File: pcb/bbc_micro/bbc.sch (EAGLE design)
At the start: 16 parts, among them J1 ATX24RH

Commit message: added one more -5v rail
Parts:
- added U$5: BLADE28, blade:BLADE28
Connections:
- net N$2: now also U$5.P$1
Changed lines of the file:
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@@
 <part name="GND1" library="supply1" library_urn="urn:adsk.eagle:library:371" deviceset="GND" device=""/>
 <part name="P+2" library="supply1" library_urn="urn:adsk.eagle:library:371" deviceset="+5V" device=""/>
+<part name="U$5" library="blade" deviceset="BLADE28" device=""/>
 </parts>
 <sheets>
@@
 <attribute name="VALUE" x="-12.7" y="165.1" size="1.778" layer="96" rot="R90"/>
 </instance>
+<instance part="U$5" gate="G$1" x="185.42" y="101.6" smashed="yes"/>
 </instances>
 <busses>
@@
 <junction x="157.48" y="96.52"/>
 <pinref part="U$2" gate="G$1" pin="P$1"/>
-<wire x1="157.48" y1="96.52" x2="175.26" y2="96.52" width="0.1524" layer="91"/>
-</segment>
-</net>
+<wire x1="157.48" y1="96.52" x2="170.18" y2="96.52" width="0.1524" layer="91"/>
+<pinref part="U$5" gate="G$1" pin="P$1"/>
+<wire x1="170.18" y1="96.52" x2="175.26" y2="96.52" width="0.1524" layer="91"/>
+<wire x1="175.26" y1="101.6" x2="170.18" y2="101.6" width="0.1524" layer="91"/>
+<wire x1="170.18" y1="101.6" x2="170.18" y2="96.52" width="0.1524" layer="91"/>
+<junction x="170.18" y="96.52"/>
+</segment>
+</net>

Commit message: BBC micro USB adaptor
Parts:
- removed IC1: (no value), v-reg:79XXS
- removed J1: ATX24RH, macse:ATX24RH
- removed JP2: (no value), pinhead:PINHD-1X3
- removed U$1: CAR_FUSE_HOLDER3IN1, atx_power_control:CAR_FUSE_HOLDER3IN1
- removed U$2: BLADE28, blade:BLADE28
- added C1, C8: 100nF, clock:CAP0805
- added C2, C4, C6: 1uF, clock:CAP0805
- added C5: 2.2uF, clock:CAP0805
- added C7: (no value), adafruit:CPOL-USE2.5-6
- added R1, R2: 5K1, atx_power_control:RESISTOR0805-RES
- added U1, U3: TPS60400DVBR, TPS6040x:TPS60400DVBR
- added U2: USBC_16P, my_usbc_16p:USBC_16P
- C3: value (none) -> 1uF; device capacitor-wima:C5/2.5 -> clock:CAP0805
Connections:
- removed net +12V: J1.12V@0, JP2.3
- removed net -12V: IC1.IN, J1.-12V
- removed net N$6: J1.5V@1, J1.5V@2, J1.5V@3, J1.5V@4, JP2.1, U$1.B0, U$1.B1
- new net -5V: C5.1, C8.2, U$5.P$1, U1.OUT, U3.OUT
- new net N$3: C3.1, U3.C1+
- new net N$31: R1.1, U2.CC2
- new net N$33: R2.1, U2.CC1
- new net N$4: C4.2, U1.C1-
- net +5V: now also C1.2, C2.2, C6.2, C7.+, JP1.1, JP3.2_VCC, U$3.P$2, U$3.P$4, U1.IN, U3.IN; no longer U$1.A0, U$1.A1
- net GND: now also C1.1, C2.1, C5.2, C6.1, C7.-, C8.1, R1.2, R2.2, U1.GND, U2.GND, U3.GND; no longer C3.2, IC1.GND, J1.GND@0, J1.GND@1, J1.GND@2, J1.GND@3, J1.GND@4, J1.GND@5, J1.GND@6, J1.GND@7, JP1.2, U$3.P$1, U$3.P$3
- net N$1: now also JP1.2, U$3.P$1, U$3.P$3, U2.VBUS; no longer JP2.2, JP3.2_VCC
- net N$2: now also C3.2, U3.C1-; no longer C3.1, IC1.OUT, U$2.P$1, U$5.P$1
- net N$5: now also C4.1, U1.C1+; no longer J1.PS_ON, JP1.1, U$3.P$2, U$3.P$4
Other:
- moved on the sheet: C3, JP1

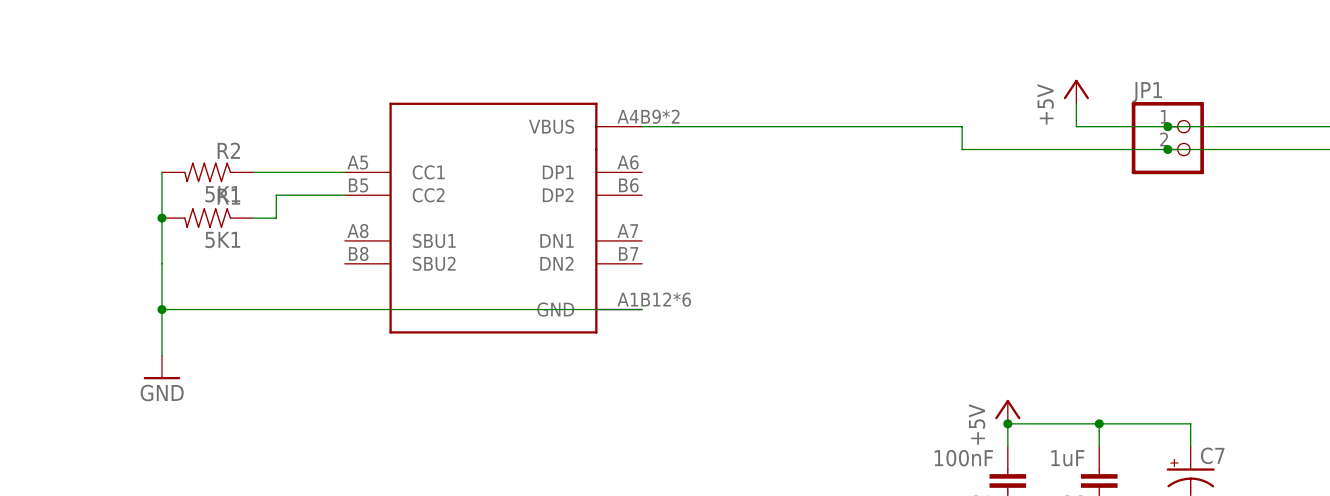
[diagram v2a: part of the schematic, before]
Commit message: BBC micro USB adaptor
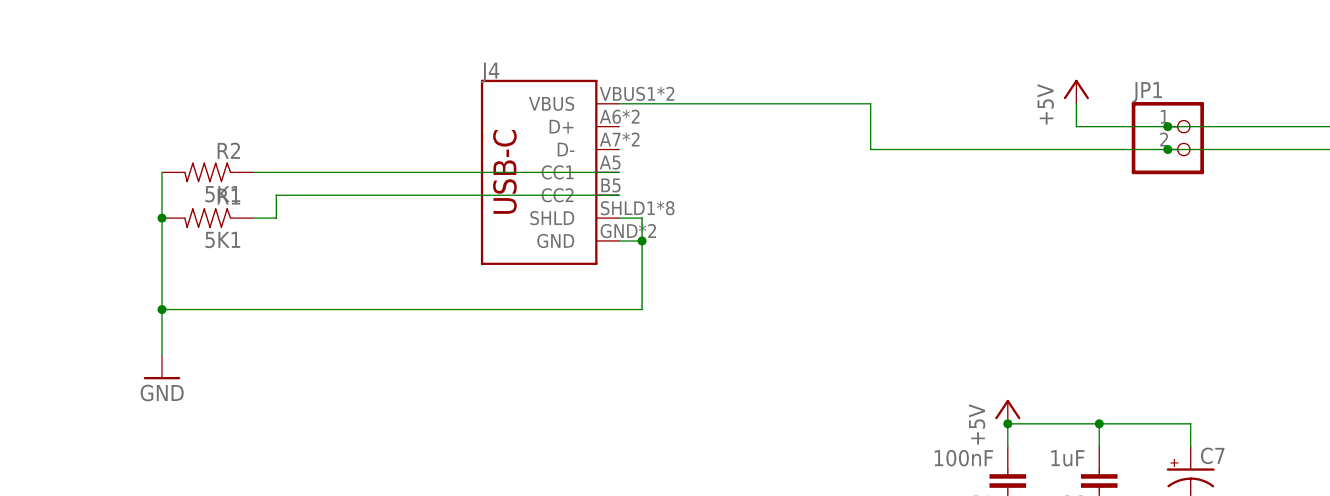
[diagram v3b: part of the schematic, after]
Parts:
- removed U2: USBC_16P, my_usbc_16p:USBC_16P
- added J4: (no value), SparkFun-Connectors:USB_C16PIN
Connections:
- removed net N$33: R2.1, U2.CC1
- new net N$6: J4.CC1, R2.1
- net GND: now also J4.GND, J4.SHLD; no longer U2.GND
- net N$1: now also J4.VBUS; no longer U2.VBUS
- net N$31: now also J4.CC2; no longer U2.CC2
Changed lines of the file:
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@@
 <part name="P+2" library="supply1" library_urn="urn:adsk.eagle:library:371" deviceset="+5V" device=""/>
 <part name="U$5" library="blade" deviceset="BLADE28" device=""/>
-<part name="U2" library="my_usbc_16p" deviceset="USBC_16P" device=""/>
 <part name="GND6" library="supply1" deviceset="GND" device=""/>
 <part name="R1" library="atx_power_control" deviceset="RESISTOR" device="0805-RES" value="5K1"/>
@@
 <part name="C8" library="clock" deviceset="CAP" device="0805" value="100nF"/>
 <part name="GND4" library="supply1" library_urn="urn:adsk.eagle:library:371" deviceset="GND" device=""/>
+<part name="J4" library="SparkFun-Connectors" deviceset="USB_C" device="16PIN"/>
 </parts>
 <sheets>
@@
 </instance>
 <instance part="U$5" gate="G$1" x="401.32" y="175.26" smashed="yes"/>
-<instance part="U2" gate="G$1" x="91.44" y="193.04" smashed="yes" rot="MR0"/>
 <instance part="GND6" gate="1" x="53.34" y="185.42" smashed="yes" rot="MR0">
 <attribute name="VALUE" x="55.88" y="182.88" size="1.778" layer="96" rot="MR0"/>
@@
 <instance part="GND4" gate="1" x="383.54" y="165.1" smashed="yes">
 <attribute name="VALUE" x="381" y="162.56" size="1.778" layer="96"/>
+</instance>
+<instance part="J4" gate="J1" x="91.44" y="208.28" smashed="yes">
+<attribute name="VALUE" x="88.9" y="195.834" size="1.778" layer="96" font="vector" rot="MR180" align="top-left"/>
+<attribute name="NAME" x="88.9" y="218.694" size="1.778" layer="95" font="vector"/>
 </instance>
 </instances>
@@
 <segment>
 <pinref part="GND6" gate="1" pin="GND"/>
-<wire x1="53.34" y1="198.12" x2="53.34" y2="193.04" width="0.1524" layer="91"/>
 <pinref part="R1" gate="G$1" pin="2"/>
-<wire x1="53.34" y1="193.04" x2="53.34" y2="187.96" width="0.1524" layer="91"/>
-<wire x1="53.34" y1="203.2" x2="53.34" y2="198.12" width="0.1524" layer="91"/>
+<wire x1="53.34" y1="203.2" x2="53.34" y2="193.04" width="0.1524" layer="91"/>
 <junction x="53.34" y="203.2"/>
 <pinref part="R2" gate="G$1" pin="2"/>
+<wire x1="53.34" y1="193.04" x2="53.34" y2="187.96" width="0.1524" layer="91"/>
 <wire x1="53.34" y1="208.28" x2="53.34" y2="203.2" width="0.1524" layer="91"/>
-<pinref part="U2" gate="G$1" pin="GND"/>
-<wire x1="106.68" y1="193.04" x2="53.34" y2="193.04" width="0.1524" layer="91"/>
+<wire x1="53.34" y1="193.04" x2="106.68" y2="193.04" width="0.1524" layer="91"/>
+<wire x1="106.68" y1="193.04" x2="106.68" y2="200.66" width="0.1524" layer="91"/>
 <junction x="53.34" y="193.04"/>
+<pinref part="J4" gate="J1" pin="SHLD"/>
+<wire x1="106.68" y1="200.66" x2="106.68" y2="203.2" width="0.1524" layer="91"/>
+<wire x1="106.68" y1="203.2" x2="104.14" y2="203.2" width="0.1524" layer="91"/>
+<pinref part="J4" gate="J1" pin="GND"/>
+<wire x1="104.14" y1="200.66" x2="106.68" y2="200.66" width="0.1524" layer="91"/>
+<junction x="106.68" y="200.66"/>
 </segment>
 <segment>
@@
 <pinref part="R1" gate="G$1" pin="1"/>
 <wire x1="66.04" y1="203.2" x2="63.5" y2="203.2" width="0.1524" layer="91"/>
-<wire x1="73.66" y1="205.74" x2="66.04" y2="205.74" width="0.1524" layer="91"/>
 <wire x1="66.04" y1="205.74" x2="66.04" y2="203.2" width="0.1524" layer="91"/>
-<pinref part="U2" gate="G$1" pin="CC2"/>
-</segment>
-</net>
-<net name="N$33" class="0">
-<segment>
-<pinref part="R2" gate="G$1" pin="1"/>
-<wire x1="73.66" y1="208.28" x2="63.5" y2="208.28" width="0.1524" layer="91"/>
-<pinref part="U2" gate="G$1" pin="CC1"/>
+<pinref part="J4" gate="J1" pin="CC2"/>
+<wire x1="66.04" y1="205.74" x2="104.14" y2="205.74" width="0.1524" layer="91"/>
 </segment>
 </net>
@@
 <wire x1="203.2" y1="200.66" x2="215.9" y2="200.66" width="0.1524" layer="91"/>
 <junction x="215.9" y="200.66"/>
-<pinref part="U2" gate="G$1" pin="VBUS"/>
-<wire x1="106.68" y1="213.36" x2="142.24" y2="213.36" width="0.1524" layer="91"/>
-<wire x1="142.24" y1="213.36" x2="142.24" y2="210.82" width="0.1524" layer="91"/>
-<wire x1="142.24" y1="210.82" x2="165.1" y2="210.82" width="0.1524" layer="91"/>
+<wire x1="132.08" y1="210.82" x2="165.1" y2="210.82" width="0.1524" layer="91"/>
 <junction x="165.1" y="210.82"/>
+<pinref part="J4" gate="J1" pin="VBUS"/>
+<wire x1="104.14" y1="215.9" x2="132.08" y2="215.9" width="0.1524" layer="91"/>
+<wire x1="132.08" y1="215.9" x2="132.08" y2="210.82" width="0.1524" layer="91"/>
 </segment>
 </net>
@@
 </segment>
 </net>
+<net name="N$6" class="0">
+<segment>
+<pinref part="R2" gate="G$1" pin="1"/>
+<pinref part="J4" gate="J1" pin="CC1"/>
+<wire x1="63.5" y1="208.28" x2="104.14" y2="208.28" width="0.1524" layer="91"/>
+</segment>
+</net>

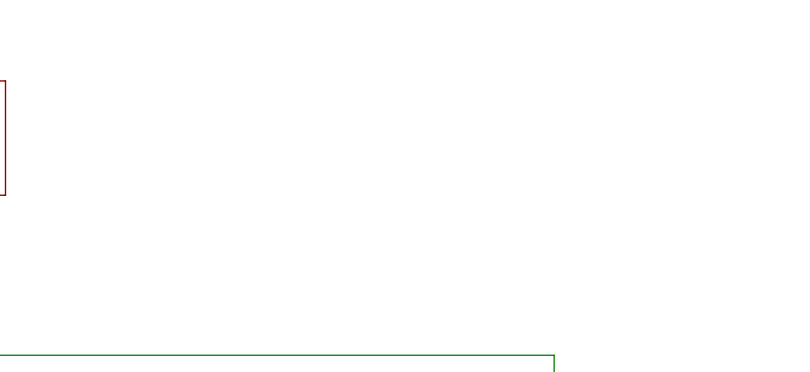
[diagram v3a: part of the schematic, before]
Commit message: updated bbc micro PCB
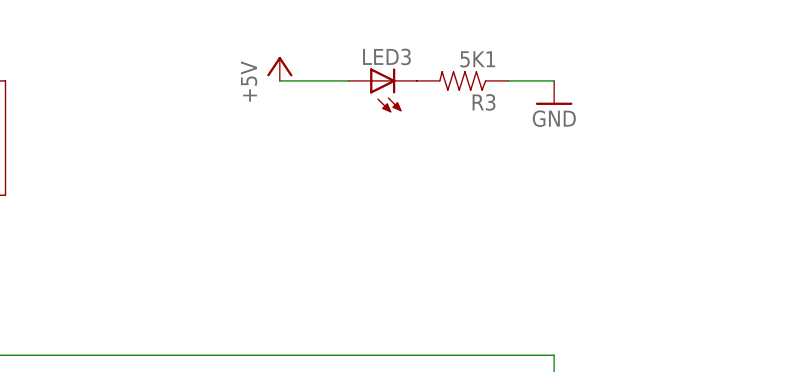
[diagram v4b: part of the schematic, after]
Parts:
- added LED3: (no value), adafruit:LEDCHIP-LED0805
- added R3: 5K1, atx_power_control:RESISTOR0805-RES
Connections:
- new net N$7: LED3.C, R3.2
- net +5V: now also LED3.A
- net GND: now also R3.1
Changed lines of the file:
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@@
 <part name="GND4" library="supply1" library_urn="urn:adsk.eagle:library:371" deviceset="GND" device=""/>
 <part name="J4" library="SparkFun-Connectors" deviceset="USB_C" device="16PIN"/>
+<part name="LED3" library="adafruit" deviceset="LED" device="CHIP-LED0805"/>
+<part name="R3" library="atx_power_control" deviceset="RESISTOR" device="0805-RES" value="5K1"/>
+<part name="GND32" library="supply1" deviceset="GND" device=""/>
+<part name="P+6" library="supply1" library_urn="urn:adsk.eagle:library:371" deviceset="+5V" device=""/>
 </parts>
 <sheets>
@@
 <attribute name="VALUE" x="88.9" y="195.834" size="1.778" layer="96" font="vector" rot="MR180" align="top-left"/>
 <attribute name="NAME" x="88.9" y="218.694" size="1.778" layer="95" font="vector"/>
+</instance>
+<instance part="LED3" gate="G$1" x="266.7" y="218.44" smashed="yes" rot="R90">
+<attribute name="NAME" x="271.272" y="221.996" size="1.778" layer="95" rot="R180"/>
+<attribute name="VALUE" x="271.272" y="224.155" size="1.778" layer="96" rot="R180"/>
+</instance>
+<instance part="R3" gate="G$1" x="276.86" y="218.44" smashed="yes" rot="R180">
+<attribute name="NAME" x="280.67" y="216.9414" size="1.778" layer="95" rot="R180"/>
+<attribute name="VALUE" x="280.67" y="221.742" size="1.778" layer="96" rot="R180"/>
+</instance>
+<instance part="GND32" gate="1" x="287.02" y="215.9" smashed="yes" rot="MR0">
+<attribute name="VALUE" x="289.56" y="213.36" size="1.778" layer="96" rot="MR0"/>
+</instance>
+<instance part="P+6" gate="1" x="256.54" y="220.98" smashed="yes">
+<attribute name="VALUE" x="254" y="215.9" size="1.778" layer="96" rot="R90"/>
 </instance>
 </instances>
@@
 <pinref part="GND4" gate="1" pin="GND"/>
 </segment>
+<segment>
+<pinref part="R3" gate="G$1" pin="1"/>
+<pinref part="GND32" gate="1" pin="GND"/>
+<wire x1="281.94" y1="218.44" x2="287.02" y2="218.44" width="0.1524" layer="91"/>
+</segment>
 </net>
 <net name="+5V" class="0">
@@
 <pinref part="JP3" gate="A" pin="2_VCC"/>
 <wire x1="35.56" y1="129.54" x2="2.54" y2="129.54" width="0.1524" layer="91"/>
+</segment>
+<segment>
+<pinref part="LED3" gate="G$1" pin="A"/>
+<pinref part="P+6" gate="1" pin="+5V"/>
+<wire x1="264.16" y1="218.44" x2="256.54" y2="218.44" width="0.1524" layer="91"/>
 </segment>
 </net>
@@
 </segment>
 </net>
+<net name="N$7" class="0">
+<segment>
+<pinref part="LED3" gate="G$1" pin="C"/>
+<pinref part="R3" gate="G$1" pin="2"/>
+</segment>
+</net>
